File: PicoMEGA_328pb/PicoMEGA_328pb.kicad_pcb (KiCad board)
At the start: 2 copper layers, 25 x 23.5 mm, 26 parts, among them J1 ICSP, J2 3V3, J3 GPIO BLK A, J4 GPIO BLK B, J5 GPIO BLK C, J6 GPIO BLK D, U1 TPS62745DSSR, U2 ATmega328PB-MU, Y1 8Mhz

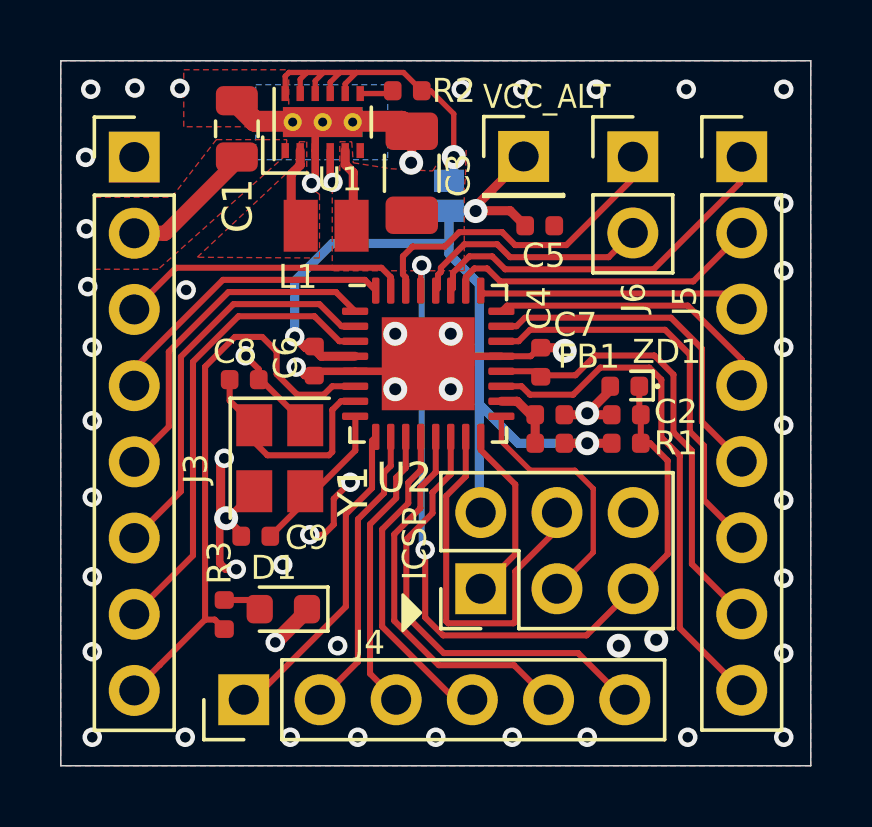
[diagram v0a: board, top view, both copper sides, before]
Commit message: PicoMEGA 328PB: rev0.1d
Fixed V_in regulator to use input voltage for enable to gurantee the
regulator powers on when an input voltage is applied.
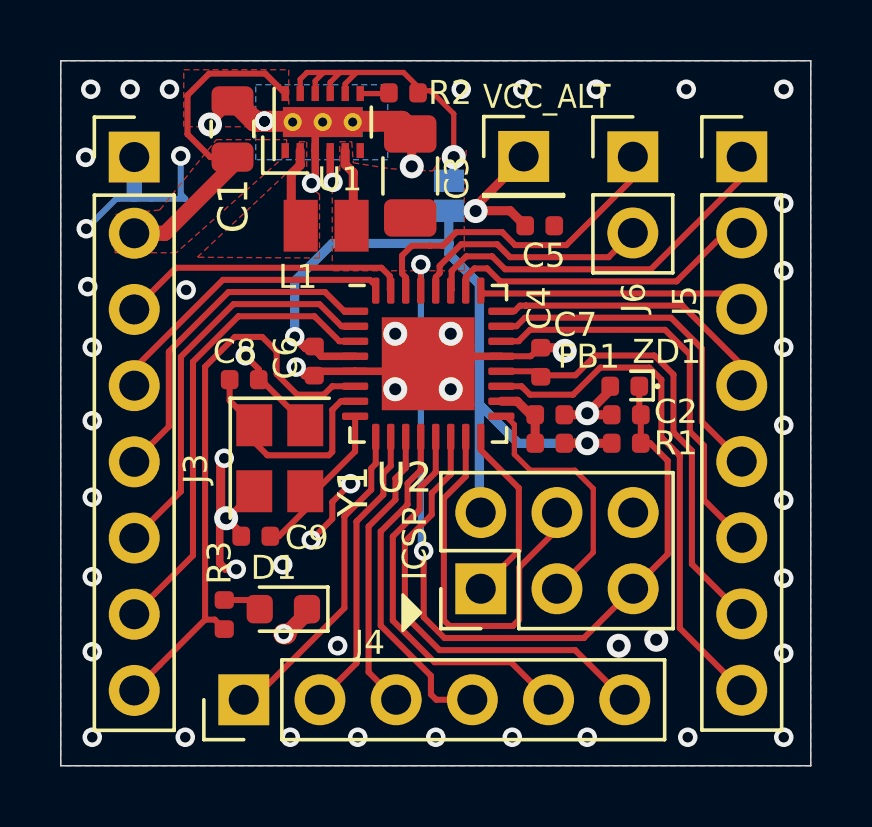
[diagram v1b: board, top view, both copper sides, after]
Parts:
- moved C1 0.15 mm to (140.2, 92.3)
- moved R2 0.14 mm to (145.9, 91.1)
- moved C3 0.10 mm to (146.2, 93.8)
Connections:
- U1 pad 12: /3V3_REG -> +9V
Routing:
- net GND: track 37.0 -> 44.1 mm, vias 54 -> 58
- net +9V: track 4.45 -> 11.4 mm
- net /3V3_REG: track 15.4 -> 14.1 mm
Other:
- board text added: "PicoMEGA 328PB Rev 0.1d Jun 2020"
- board text removed: "PicoMEGA 328PB Rev 0.1c Jun 2020"

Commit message: PicoMEGA 328PB: rev0.1e
Revised clock area to use guard ring to prevent cross-talk interference
for adjacent GPIO traces. No such protection of the GPIOs themselves
though.
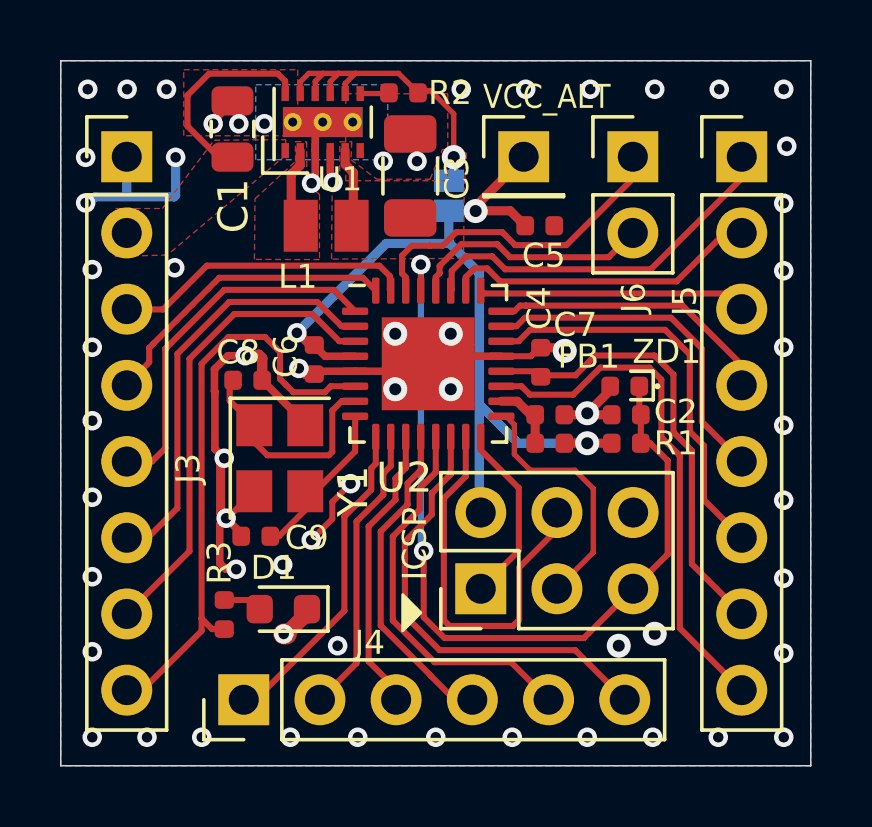
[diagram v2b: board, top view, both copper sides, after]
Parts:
- moved J3 0.25 mm to (136.7, 93.2)
- moved C8 0.12 mm to (140.7, 100.7)
- moved C6 0.05 mm to (142.9, 100.0)
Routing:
- net +9V: track 11.4 -> 7.03 mm
- net GND: track 44.1 -> 40.7 mm, vias 58 -> 63
- net +3V3: track 32.2 -> 31.0 mm
- net /PD3: track 11.4 -> 12.4 mm
- net /PE1: track 19.3 -> 20.0 mm
- net /PD4: track 13.5 -> 14.2 mm
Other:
- board text added: "PicoMEGA 328PB Rev 0.1e Jun 2020"
- board text removed: "PicoMEGA 328PB Rev 0.1d Jun 2020"
